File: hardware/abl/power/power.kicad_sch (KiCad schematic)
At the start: 29 parts, among them J1 Screw_Terminal_01x03, J2 Screw_Terminal_01x03, J3 009159008603906, U1 TWGMC AMS1117-3.3, U2 TMP1075D, U3 INA219AxD

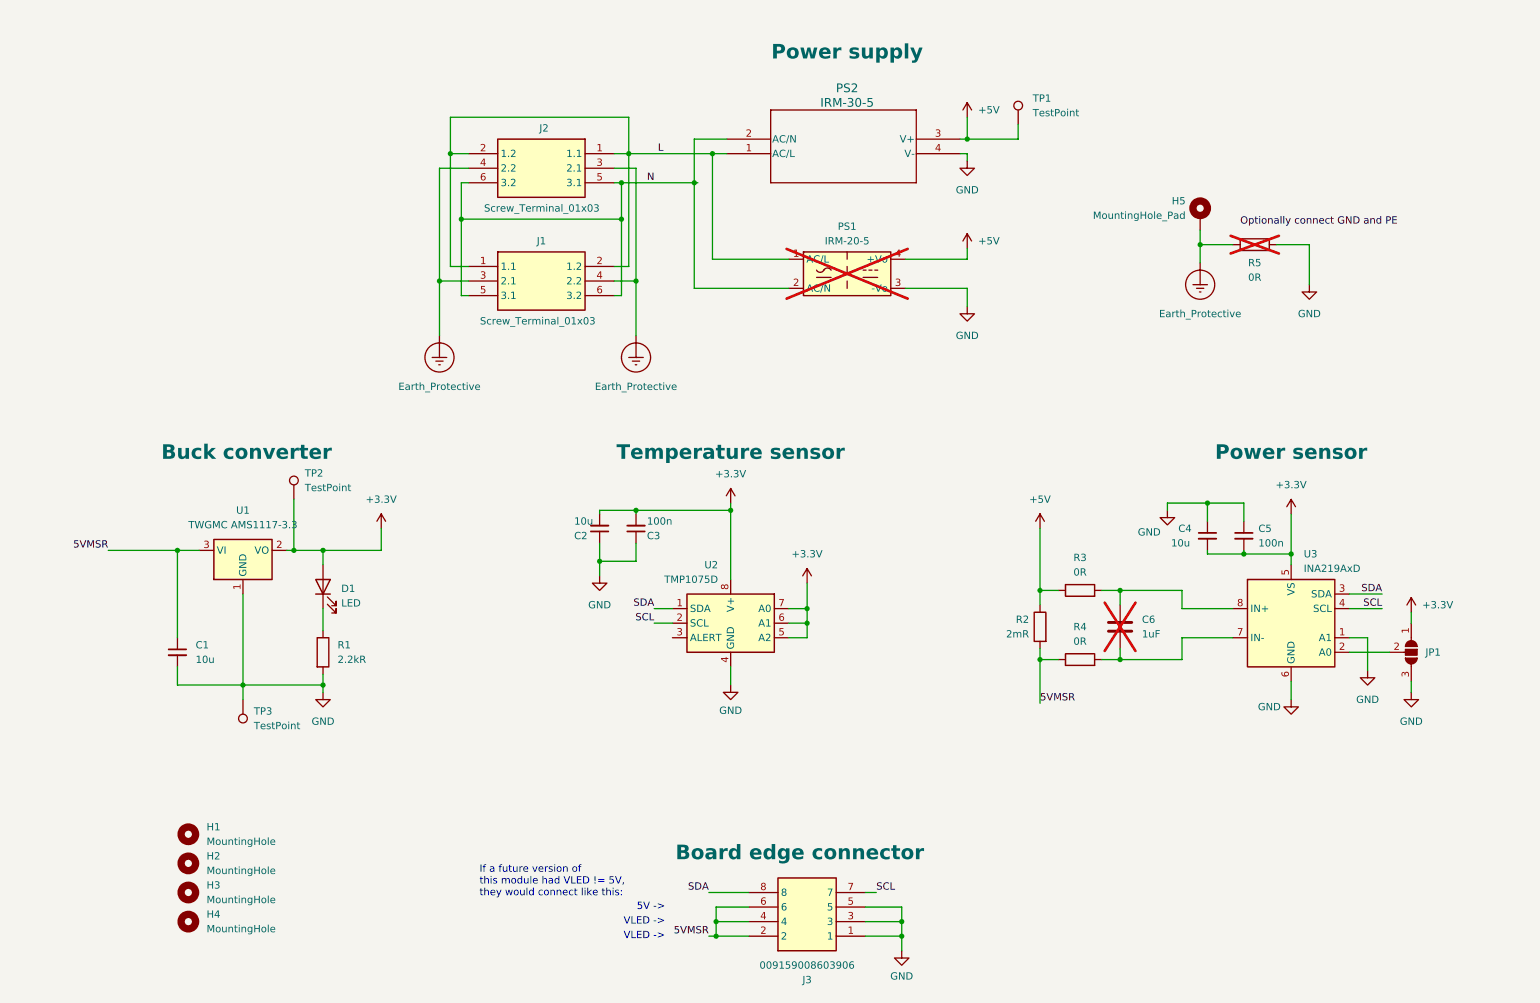
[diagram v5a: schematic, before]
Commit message: More minor optimizatios, add meta data.
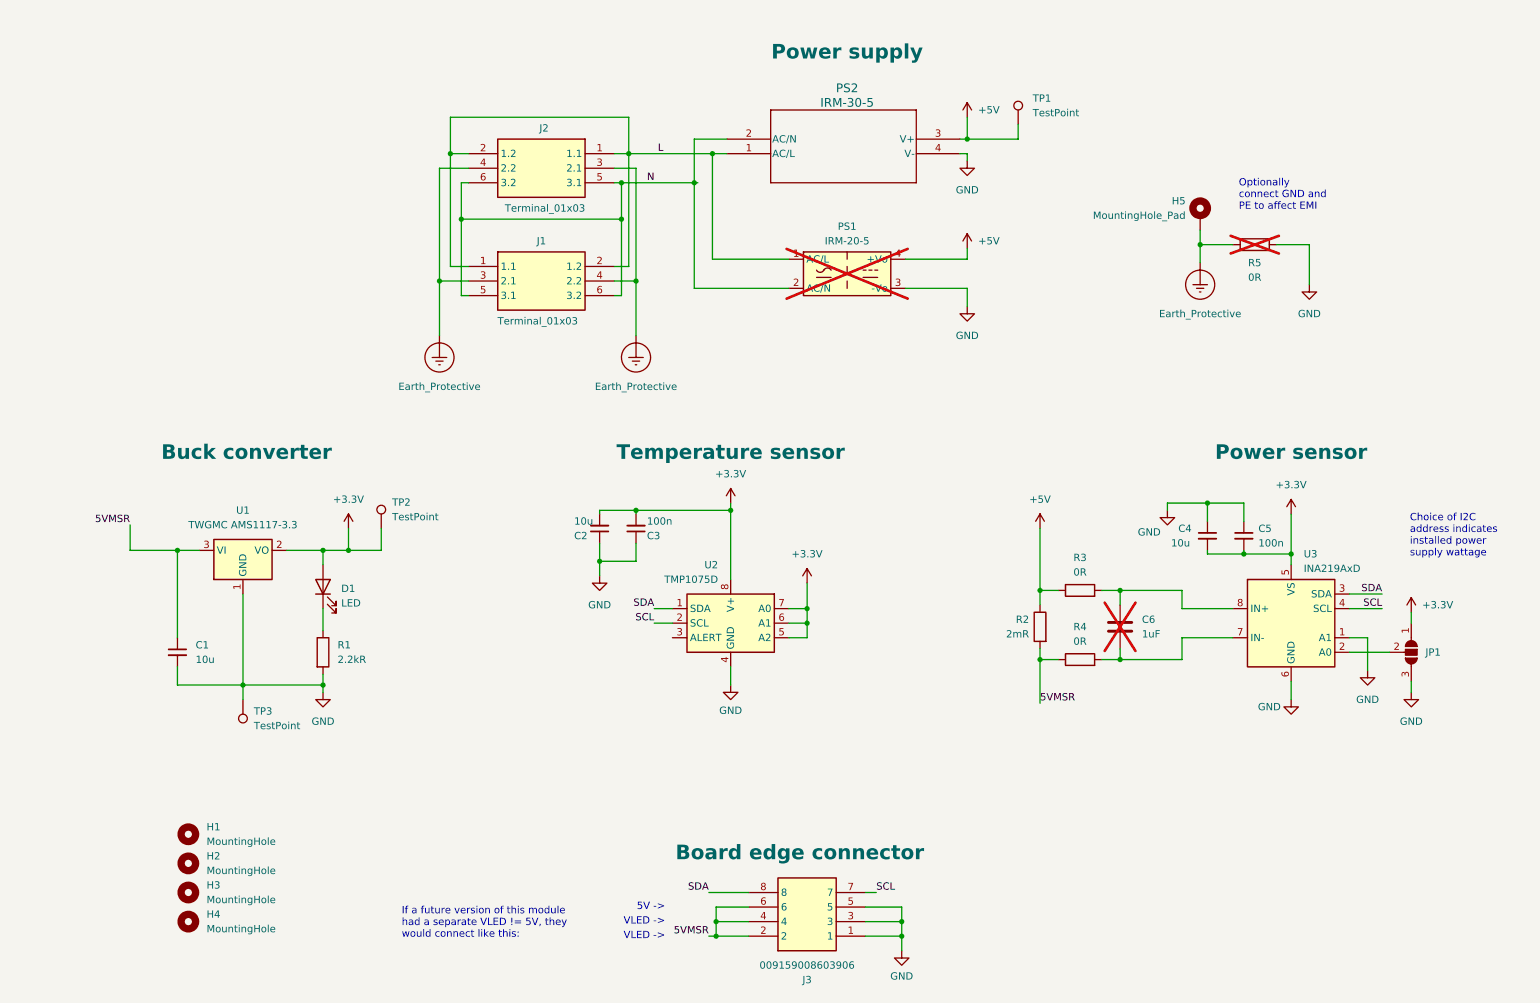
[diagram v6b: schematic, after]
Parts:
- J1, J2: value Screw_Terminal_01x03 -> Terminal_01x03
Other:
- note removed: "If a future version of this module had VLED != 5V, they would connect like this:"
- title: (none) -> besteLampe! ABL Power Moudule
- moved on the sheet: TP2
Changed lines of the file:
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@@
 	(generator_version "8.0")
 	(paper "A4")
+	(title_block
+		(title "besteLampe! ABL Power Moudule")
+		(date "2024-10-01")
+		(rev "1.0")
+		(comment 1 "See  https://lenaschimmel.de/besteLampe! for the source and more information")
+		(comment 2 "This source describes Open Hardware and is licensed under the CERN-OHL-S v2.")
+		(comment 3 "Copyright 2024 Lena Schimmel <mail@lenaschimmel.de>")
+		(comment 4 "Design for JLCPCB 1-2 Layer Service")
+	)
 	(junction
 		(at 121.285 55.88)
@@
 	)
 	(junction
-		(at 64.135 113.665)
-		(diameter 0)
-		(color 0 0 0 0)
-	)
-	(junction
 		(at 208.28 120.65)
 		(diameter 0)
@@
 	)
 	(junction
+		(at 73.66 113.665)
+		(diameter 0)
+		(color 0 0 0 0)
+	)
+	(junction
 		(at 137.795 180.975)
 		(diameter 0)
@@
 	(wire
 		(pts
-			(xy 64.135 113.665) (xy 69.215 113.665)
-		)
-		(stroke
-			(width 0)
-			(type default)
-		)
-	)
-	(wire
-		(pts
 			(xy 94.615 69.215) (xy 93.345 69.215)
 		)
@@
 	(wire
 		(pts
+			(xy 35.56 109.22) (xy 35.56 113.665)
+		)
+		(stroke
+			(width 0)
+			(type default)
+		)
+	)
+	(wire
+		(pts
 			(xy 136.525 180.975) (xy 137.795 180.975)
 		)
@@
 	(wire
 		(pts
-			(xy 79.375 109.855) (xy 79.375 113.665)
+			(xy 73.66 109.855) (xy 73.66 113.665)
 		)
 		(stroke
@@
 	(wire
 		(pts
+			(xy 35.56 113.665) (xy 43.815 113.665)
+		)
+		(stroke
+			(width 0)
+			(type default)
+		)
+	)
+	(wire
+		(pts
 			(xy 120.015 64.135) (xy 122.555 64.135)
 		)
@@
 	(wire
 		(pts
+			(xy 73.66 113.665) (xy 79.375 113.665)
+		)
+		(stroke
+			(width 0)
+			(type default)
+		)
+	)
+	(wire
+		(pts
 			(xy 117.475 115.57) (xy 117.475 118.11)
 		)
@@
 	(wire
 		(pts
-			(xy 64.135 113.665) (xy 64.135 104.775)
-		)
-		(stroke
-			(width 0)
-			(type default)
-		)
-	)
-	(wire
-		(pts
-			(xy 31.75 113.665) (xy 43.815 113.665)
+			(xy 79.375 113.665) (xy 79.375 109.855)
 		)
 		(stroke
@@
 	(wire
 		(pts
-			(xy 79.375 113.665) (xy 69.215 113.665)
+			(xy 123.825 106.68) (xy 117.475 106.68)
 		)
 		(stroke
@@
 	(wire
 		(pts
-			(xy 123.825 106.68) (xy 117.475 106.68)
+			(xy 163.83 175.895) (xy 170.18 175.895)
 		)
 		(stroke
@@
 	(wire
 		(pts
-			(xy 163.83 175.895) (xy 170.18 175.895)
+			(xy 205.105 132.715) (xy 208.28 132.715)
 		)
 		(stroke
@@
 	(wire
 		(pts
-			(xy 205.105 132.715) (xy 208.28 132.715)
+			(xy 137.16 62.865) (xy 137.16 44.45)
 		)
 		(stroke
@@
 	(wire
 		(pts
-			(xy 137.16 62.865) (xy 137.16 44.45)
+			(xy 117.475 115.57) (xy 123.825 115.57)
 		)
 		(stroke
@@
 	(wire
 		(pts
-			(xy 117.475 115.57) (xy 123.825 115.57)
+			(xy 197.485 120.65) (xy 194.31 120.65)
 		)
 		(stroke
@@
 	(wire
 		(pts
-			(xy 197.485 120.65) (xy 194.31 120.65)
+			(xy 69.215 113.665) (xy 69.215 116.205)
 		)
 		(stroke
@@
 	(wire
 		(pts
-			(xy 69.215 113.665) (xy 69.215 116.205)
+			(xy 73.66 113.665) (xy 69.215 113.665)
 		)
 		(stroke
@@
 	(wire
 		(pts
-			(xy 62.865 113.665) (xy 64.135 113.665)
+			(xy 62.865 113.665) (xy 69.215 113.665)
 		)
 		(stroke
@@
 		)
 	)
-	(text "If a future version of\nthis module had VLED != 5V,\nthey would connect like this:"
+	(text_box "Choice of I2C address indicates installed power supply wattage"
 		(exclude_from_sim no)
-		(at 96.52 171.45 0)
+		(at 257.81 106.045 0)
+		(size 19.05 12.065)
+		(stroke
+			(width -0.0001)
+			(type default)
+		)
+		(fill
+			(type none)
+		)
 		(effects
 			(font
 				(size 1.27 1.27)
 			)
-			(justify left)
+			(justify left top)
+		)
+	)
+	(text_box "If a future version of this module had a separate VLED != 5V, they would connect like this:"
+		(exclude_from_sim no)
+		(at 81.915 174.625 0)
+		(size 36.195 10.16)
+		(stroke
+			(width -0.0001)
+			(type default)
+		)
+		(fill
+			(type none)
+		)
+		(effects
+			(font
+				(size 1.27 1.27)
+			)
+			(justify left top)
+		)
+	)
+	(text_box "Optionally connect GND and PE to affect EMI"
+		(exclude_from_sim no)
+		(at 227.965 47.625 0)
+		(size 19.05 8.89)
+		(stroke
+			(width -0.0001)
+			(type default)
+		)
+		(fill
+			(type none)
+		)
+		(effects
+			(font
+				(size 1.27 1.27)
+			)
+			(justify left top)
 		)
 	)
@@
 	)
 	(label "5VMSR"
-		(at 31.75 113.665 180)
+		(at 35.56 109.22 180)
 		(fields_autoplaced yes)
 		(effects
@@
 		)
 	)
-	(label "Optionally connect GND and PE"
-		(at 229.235 57.15 0)
-		(fields_autoplaced yes)
-		(effects
-			(font
-				(size 1.27 1.27)
-			)
-			(justify left bottom)
-		)
-	)
 	(label "SDA"
 		(at 127 123.825 180)
@@
 	(symbol
 		(lib_id "power:+3.3V")
-		(at 79.375 109.855 0)
+		(at 73.66 109.855 0)
 		(unit 1)
 		(exclude_from_sim no)
@@
 		(fields_autoplaced yes)
 		(property "Reference" "#PWR017"
-			(at 79.375 113.665 0)
+			(at 73.66 113.665 0)
 			(effects
 				(font
@@
 		)
 		(property "Value" "+3.3V"
-			(at 79.375 104.775 0)
+			(at 73.66 104.775 0)
 			(effects
 				(font
@@
 		)
 		(property "Footprint" ""
-			(at 79.375 109.855 0)
+			(at 73.66 109.855 0)
 			(effects
 				(font
@@
 		)
 		(property "Datasheet" ""
-			(at 79.375 109.855 0)
+			(at 73.66 109.855 0)
 			(effects
 				(font
@@
 		)
 		(property "Description" "Power symbol creates a global label with name \"+3.3V\""
-			(at 79.375 109.855 0)
+			(at 73.66 109.855 0)
 			(effects
 				(font
@@
 	(symbol
 		(lib_id "Connector:TestPoint")
-		(at 64.135 104.775 0)
+		(at 79.375 109.855 0)
 		(unit 1)
 		(exclude_from_sim no)
@@
 		(on_board yes)
 		(dnp no)
-		(fields_autoplaced yes)
 		(property "Reference" "TP2"
-			(at 66.04 100.2029 0)
+			(at 81.28 105.2829 0)
 			(effects
 				(font
@@
 		)
 		(property "Value" "TestPoint"
-			(at 66.04 102.7429 0)
+			(at 81.28 107.8229 0)
 			(effects
 				(font
@@
 		)
 		(property "Footprint" "TestPoint:TestPoint_THTPad_D1.0mm_Drill0.5mm"
-			(at 69.215 104.775 0)
+			(at 84.455 109.855 0)
 			(effects
 				(font
@@
 		)
 		(property "Datasheet" "~"
-			(at 69.215 104.775 0)
+			(at 84.455 109.855 0)
 			(effects
 				(font
@@
 		)
 		(property "Description" "test point"
-			(at 64.135 104.775 0)
+			(at 79.375 109.855 0)
 			(effects
 				(font
@@
 		)
 		(property "Purpose" ""
-			(at 64.135 104.775 0)
+			(at 79.375 109.855 0)
 			(effects
 				(font
@@
 			)
 		)
-		(property "Value" "Screw_Terminal_01x03"
+		(property "Value" "Terminal_01x03"
 			(at 106.68 73.66 0)
 			(effects
@@
 			)
 		)
-		(property "Value" "Screw_Terminal_01x03"
-			(at 117.475 53.975 0)
+		(property "Value" "Terminal_01x03"
+			(at 107.95 53.975 0)
 			(effects
 				(font
 					(size 1.27 1.27)
 				)
-				(justify left)
 			)
 		)

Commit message: Metadata and minor cleanup, documentation and typo fix.
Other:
- title: besteLampe! ABL Power Moudule -> besteLampe! ABL Power Module
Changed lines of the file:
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@@
 	(paper "A4")
 	(title_block
-		(title "besteLampe! ABL Power Moudule")
+		(title "besteLampe! ABL Power Module")
 		(date "2024-10-01")
 		(rev "1.0")

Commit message: Implemented proposed changes.
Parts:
- added C7: 33uF, Capacitor_Tantalum_SMD:CP_EIA-3528-21_Kemet-B, symbol Device:C_Small
- C1: value 10u -> 33uF; footprint Capacitor_SMD:C_0402_1005Metric -> Capacitor_Tantalum_SMD:CP_EIA-3528-21_Kemet-B; LCSC Part C15525 -> C308920; Manufacturer_Part_Number CL05A106MQ5NUNC -> TPSB336M016R0350; Purpose (none) -> Input bypass
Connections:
- net +3.3V: now also C7.1
- net GND: now also C7.2
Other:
- moved on the sheet: D1, R1, TP2
